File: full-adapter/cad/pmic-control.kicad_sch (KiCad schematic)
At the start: 4 parts, among them U5 RK809-5

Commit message: Capture RK809 control and RTC with verified crystal lands
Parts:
- added C483, C484, C487: 1uF, Capacitor_SMD:C_0402_1005Metric, symbol Device:C
- added C485, C486: 100nF, Capacitor_SMD:C_0402_1005Metric, symbol Device:C
- added C488, C489: 22pF, Capacitor_SMD:C_0402_1005Metric, symbol Device:C
- added R490, R491: 22R 1%, Resistor_SMD:R_0402_1005Metric, symbol Device:R_Small_US
- added R492, R493: 2.2kR 1%, Resistor_SMD:R_0402_1005Metric, symbol Device:R_Small_US
- added R494, R495: 10kR 1%, Resistor_SMD:R_0402_1005Metric, symbol Device:R_Small_US
- added R496: 100kR 1%, Resistor_SMD:R_0402_1005Metric, symbol Device:R_Small_US
- added R497: 56kR 1%, Resistor_SMD:R_0402_1005Metric, symbol Device:R_Small_US
- added unit 10 of U5
- added Y490: 32.768kHz / 12.5pF, full-adapter:Epson_FC-135R_3.2x1.5mm, symbol Device:Crystal
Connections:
- net GND: now also C483.2, C484.2, C485.2, C486.2, C487.2, C488.2, C489.2, R497.2, U5.47 (GNDREF), U5.56 (BATDIV), U5.62 (SNSP), U5.63 (SNSN), U5.69 (GND)
- net VCC3V3_SYS: now also C483.1, R496.1, U5.45 (VCC_RTC)
- new net I2C0_SCL_PMIC: R490.1, R492.2
- new net I2C0_SDA_PMIC: R491.1, R493.2
- new net PMIC_INT_L: R495.2, U5.7 (~{INT})
- new net PMIC_PWRON_L: C485.1, U5.52 (~{PWRON})
- new net PMIC_SLEEP_H: U5.49 (SLEEP)
- new net RK809_SCL: R490.2, U5.1 (SCL)
- new net RK809_SDA: R491.2, U5.2 (SDA)
- new net RK809_VDC: C487.1, R496.2, R497.1, U5.61 (VDC)
- new net RK809_VREF: C484.1, U5.46 (VREF)
- new net RK809_XIN: C488.1, U5.50 (XIN), Y490.1
- new net RK809_XOUT: C489.1, U5.51 (XOUT), Y490.2
- new net SYS_RESET_L: C486.1, R494.2, U5.67 (~{RESET})
- new net VCC1V8_PMU: R492.1, R493.1
- new net VCC3V3_PMU: R494.1, R495.1
- no-connect marks 11 -> 13
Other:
- note added: "32.768kHz RTC — keep away from switching nodes"
- note added: "Delayed auto-start"
- note added: "I2C0 / PMUIO2: 1.8V. INT/reset: 3.3V PMU domain. Processor connections remain in progress. RTC 22pF loads assume about 1.5pF stray; verify startup margin, drive level and frequency."
- note added: "RK809-5 control — PMU I/O levels"
- note added: "VDC: 1.185V, tau 35.9ms nominal. Require 3.3V supply rise <=10ms. Verify the VDC edge occurs after VCC_RTC/VCC9 are valid, including brownout recovery. PWRON uses its internal pull-up; reset retains the required 100nF capacitor."
- note removed: "RTC, system control and processor-side signals are being captured. This page is incomplete and cannot authorize fabrication."

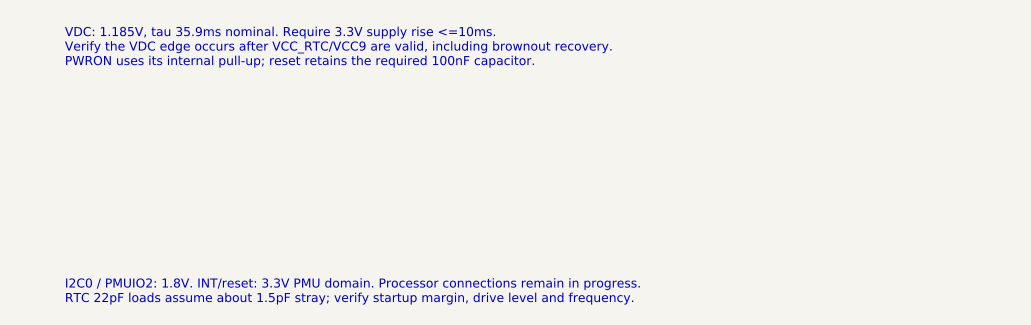
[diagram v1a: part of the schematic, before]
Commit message: Connect processor PMIC controls and hardware boot straps
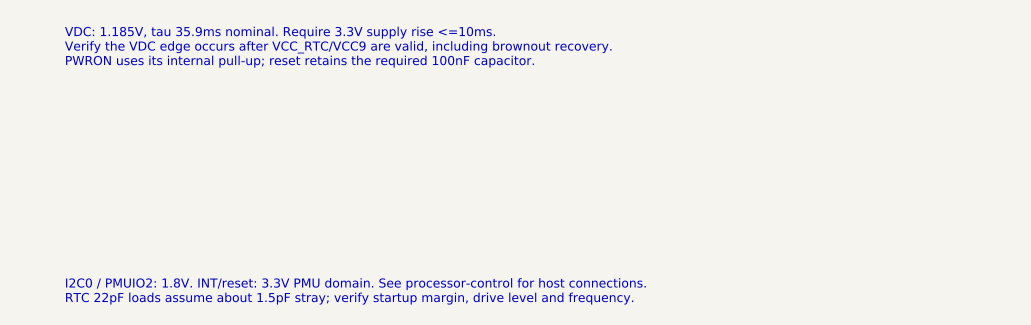
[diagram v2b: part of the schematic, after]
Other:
- note added: "I2C0 / PMUIO2: 1.8V. INT/reset: 3.3V PMU domain. See processor-control for host connections. RTC 22pF loads assume about 1.5pF stray; verify startup margin, drive level and frequency."
- note removed: "I2C0 / PMUIO2: 1.8V. INT/reset: 3.3V PMU domain. Processor connections remain in progress. RTC 22pF loads assume about 1.5pF stray; verify startup margin, drive level and frequency."
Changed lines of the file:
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@@
 (pin "1")(instances (project "full-adapter" (path "/fda20879-fa66-56c0-be14-de2506349b46/996d3e9a-d50f-5f72-b9ba-9b7221288ad0" (reference "#PWRpmiccontrol023") (unit 1)))))
 (text "VDC: 1.185V, tau 35.9ms nominal. Require 3.3V supply rise <=10ms.\nVerify the VDC edge occurs after VCC_RTC/VCC9 are valid, including brownout recovery.\nPWRON uses its internal pull-up; reset retains the required 100nF capacitor." (at 15.24 248.92 0) (effects (font (size 1.0 1.0)) (justify left top)))
-(text "I2C0 / PMUIO2: 1.8V. INT/reset: 3.3V PMU domain. Processor connections remain in progress.\nRTC 22pF loads assume about 1.5pF stray; verify startup margin, drive level and frequency." (at 15.24 276.86 0) (effects (font (size 1.0 1.0)) (justify left top)))
+(text "I2C0 / PMUIO2: 1.8V. INT/reset: 3.3V PMU domain. See processor-control for host connections.\nRTC 22pF loads assume about 1.5pF stray; verify startup margin, drive level and frequency." (at 15.24 276.86 0) (effects (font (size 1.0 1.0)) (justify left top)))
 )
